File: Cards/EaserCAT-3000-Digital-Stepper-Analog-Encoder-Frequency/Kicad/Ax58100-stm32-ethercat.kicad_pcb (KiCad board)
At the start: 2 copper layers, 94.5 x 74.4 mm, 184 parts, among them J1 Step1, J10 Encoder, J11 5V Power IN, J12 24V Field, J13 DAC, J14 In_opt1, J15 Serial usart1, J16 In_opt2, J17 STLINK, J18 Out_opt, J2 Step2, J3 Step3, J4 Step4, J5 THCAD, J6 In1-4, J7 In5-8, J8 Output1-2, J9 Output3-4, SW1 SW PB, U1 MAX3485CSA/ESA, U10 AX58100, U2 TXS0108EPW, U3 TLP292-4, U4 TLP292-4, U5 TLP292-4, U6 STM32F407VGT6, U7 AMS1117-3.3, U8 24LC32A, U9 AMS1117-1.2, Y1 8 MHz, Y2 NXK25.000AE12F-KAB6-12

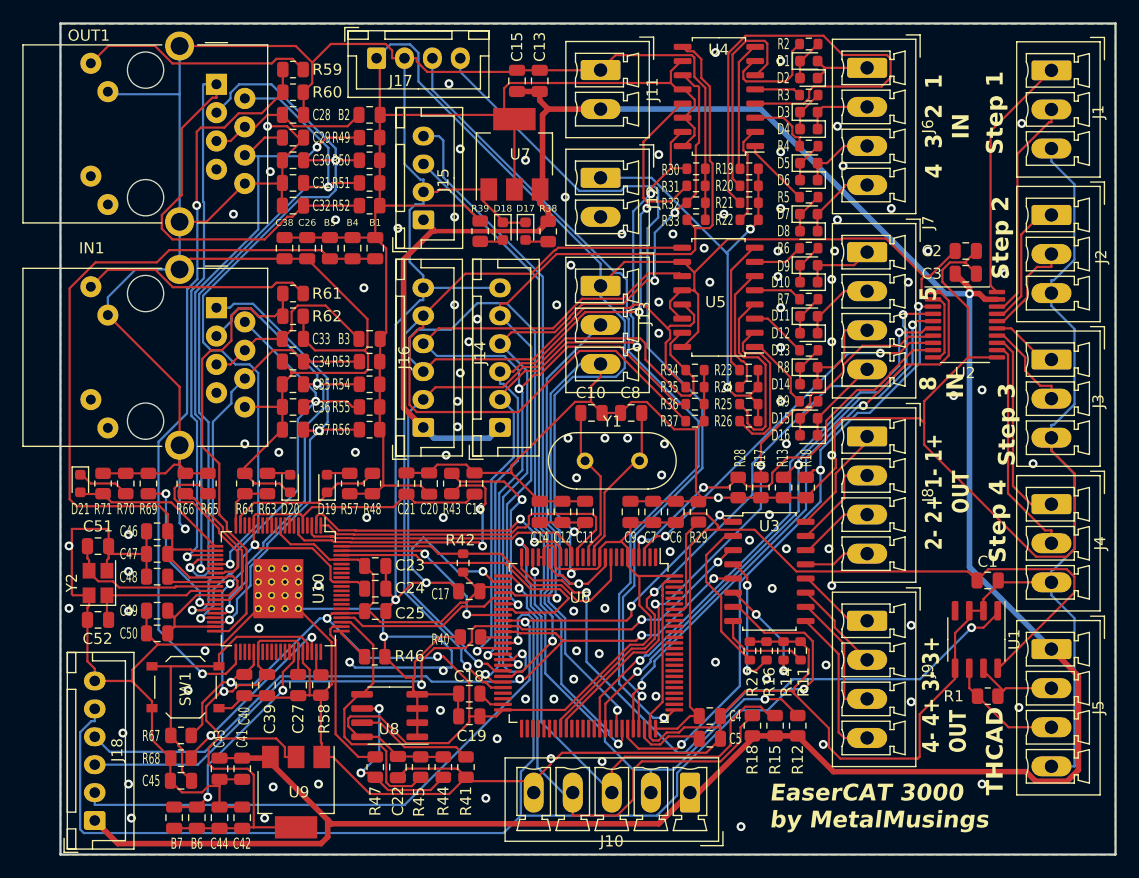
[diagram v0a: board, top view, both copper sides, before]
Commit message: Moving all to Kicad8. Housekeeping symbols,libraries,3d-models
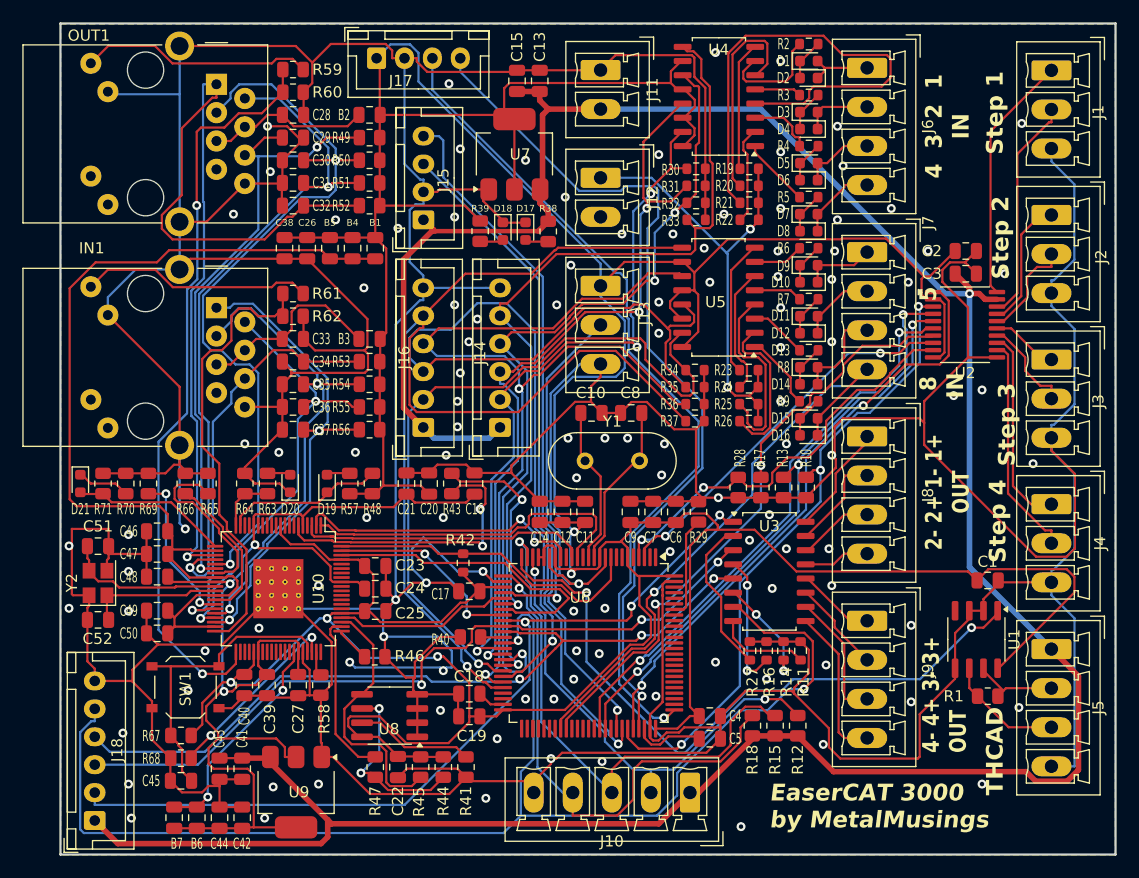
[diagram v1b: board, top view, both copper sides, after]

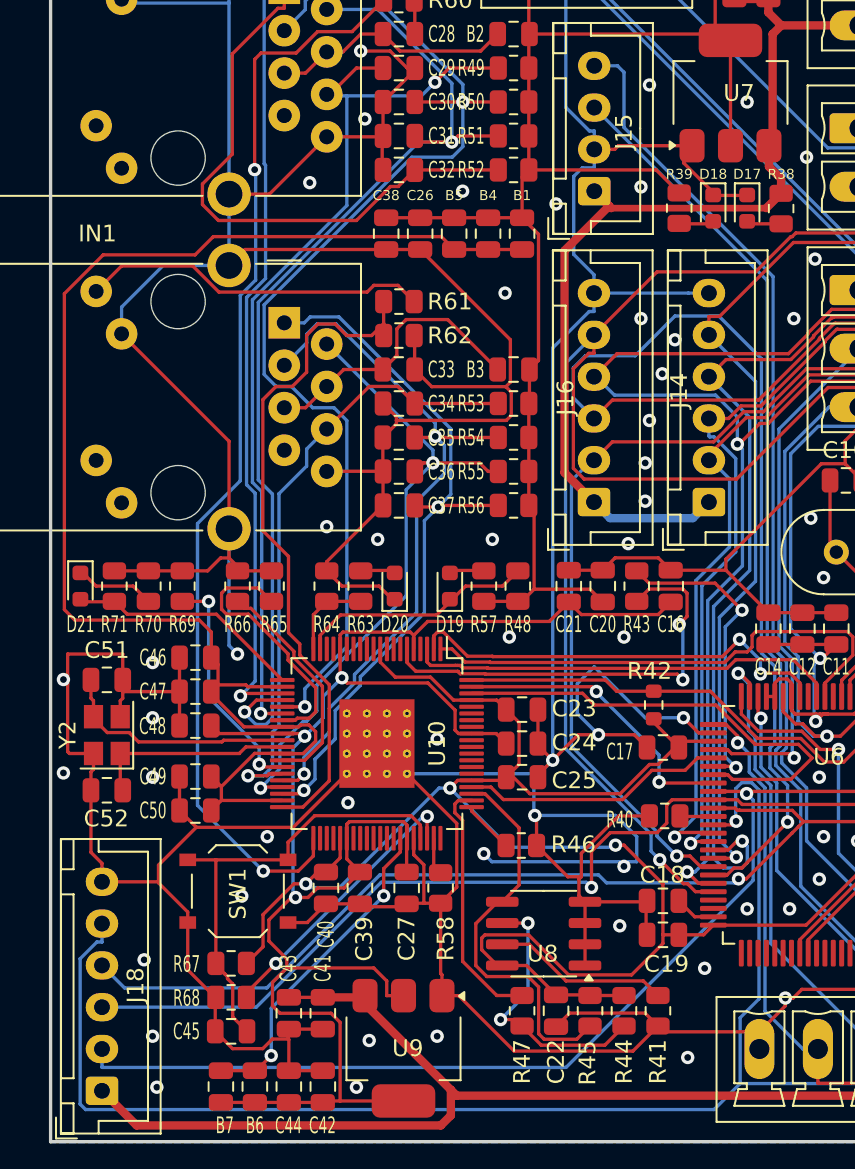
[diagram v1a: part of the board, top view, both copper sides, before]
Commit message: Updated reset circuit to PB12
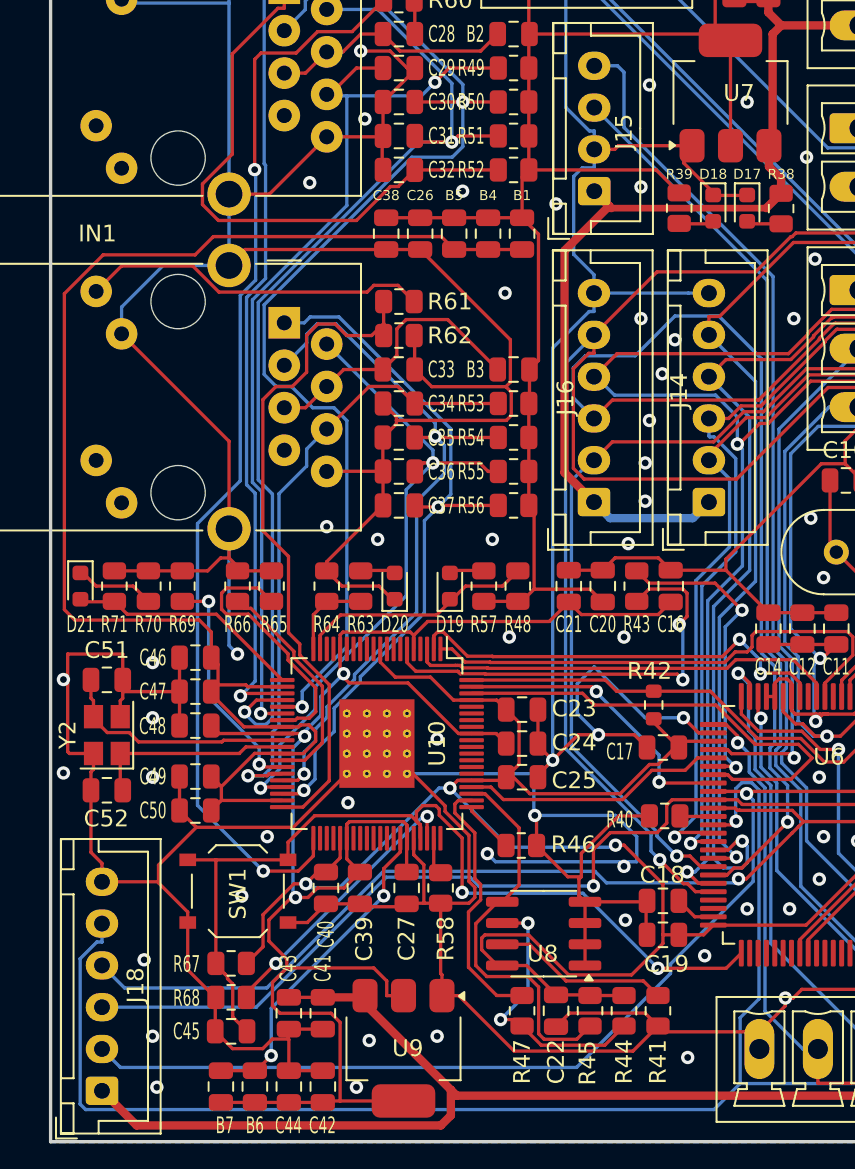
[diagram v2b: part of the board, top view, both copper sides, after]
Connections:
- U6 pad 14: RST_MCU -> unconnected-(U6-NRST-Pad14)
- U6 pad 51: unconnected-(U6-PB12-Pad51) -> RESET_MCU
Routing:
- net RESET_MCU: track 27.6 -> 55.4 mm, vias 0 -> 2
- net GND: track 829.7 -> 831.6 mm
- net Net-(U10-I2C_SCL): track 15.1 -> 15.7 mm
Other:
- board text added: "EaserCAT 3000 by MetalMusings Dec 2024"
- board text removed: "EaserCAT 3000 by MetalMusings Feb 2024 v1"
